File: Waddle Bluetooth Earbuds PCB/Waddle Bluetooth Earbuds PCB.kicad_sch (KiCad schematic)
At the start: 1 part, among them U1 DFR0781_BT401

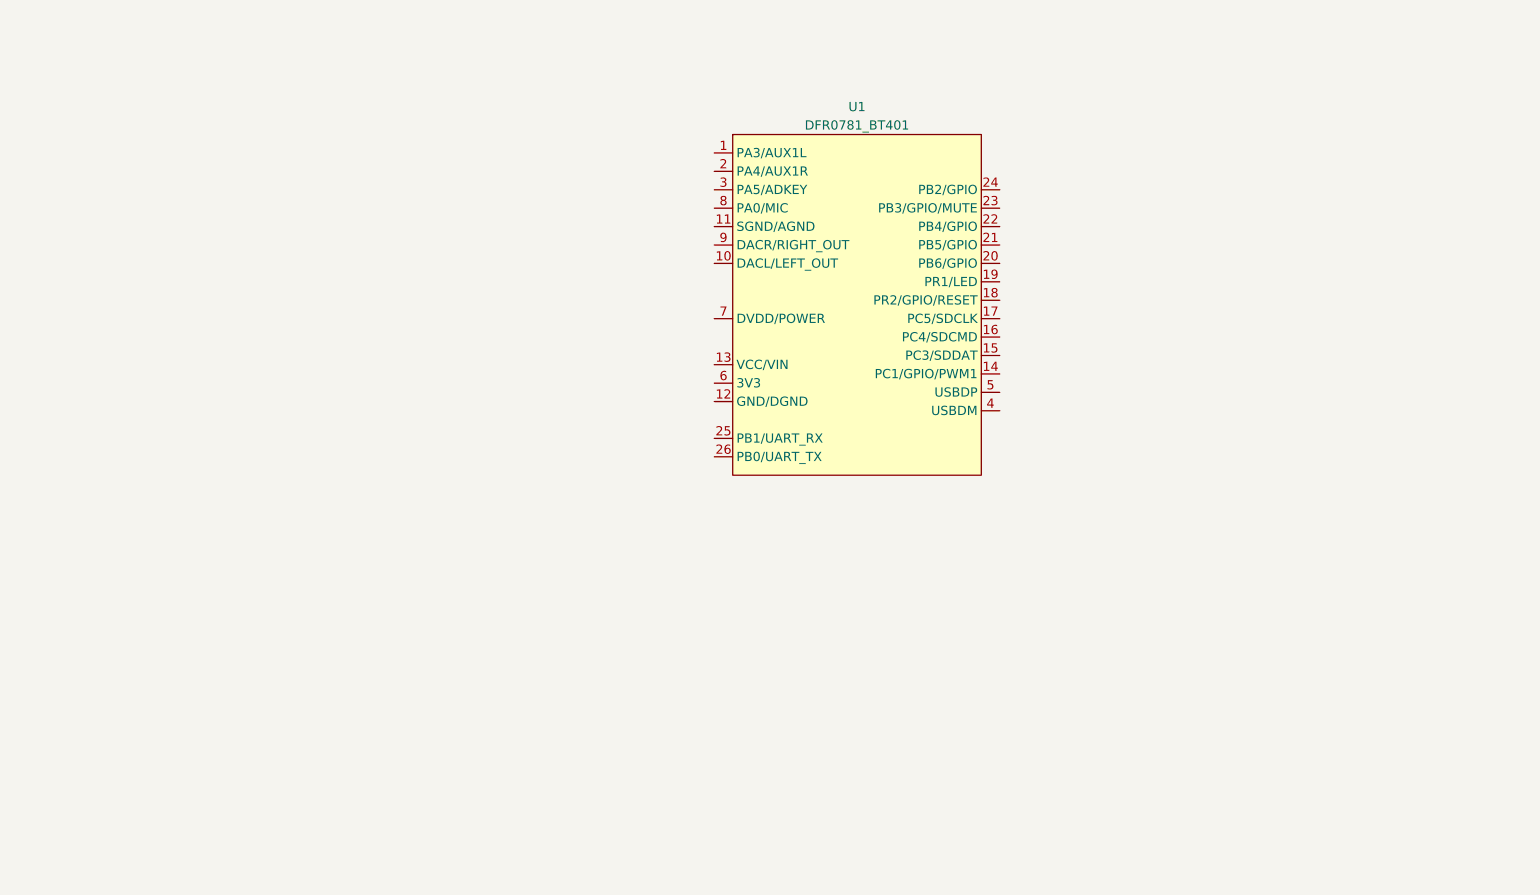
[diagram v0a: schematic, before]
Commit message: Add core bluetooth circuits
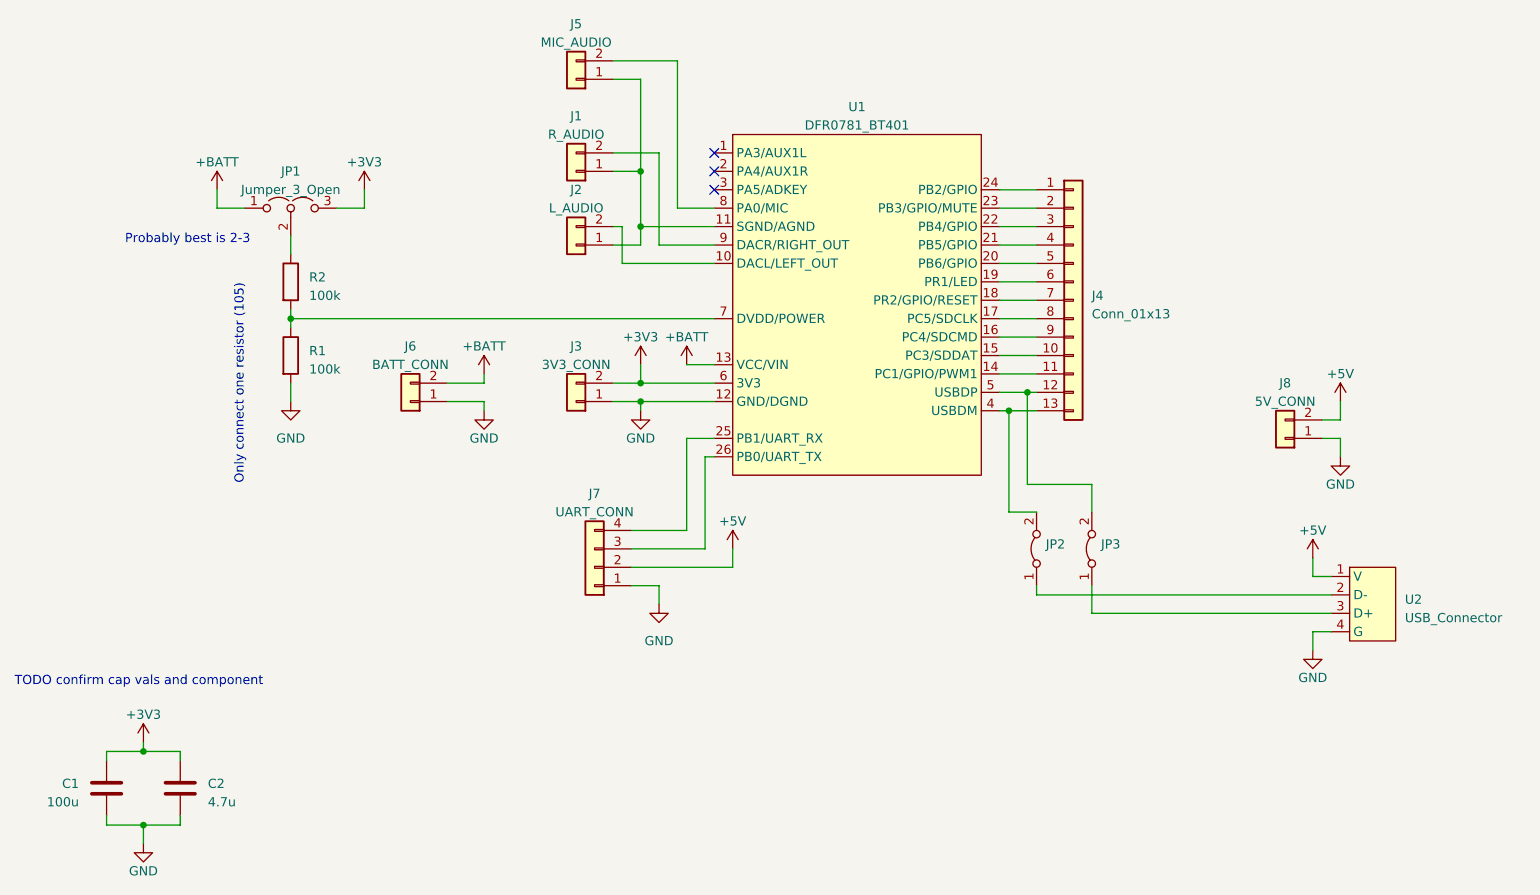
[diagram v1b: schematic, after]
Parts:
- added C1: 100u, Capacitor_SMD:C_1206_3216Metric_Pad1.33x1.80mm_HandSolder, symbol Device:C
- added C2: 4.7u, Capacitor_SMD:C_1206_3216Metric_Pad1.33x1.80mm_HandSolder, symbol Device:C
- added J1: R_AUDIO, Connector_PinHeader_1.27mm:PinHeader_1x02_P1.27mm_Vertical, symbol Connector_Generic:Conn_01x02
- added J2: L_AUDIO, Connector_PinHeader_1.27mm:PinHeader_1x02_P1.27mm_Vertical, symbol Connector_Generic:Conn_01x02
- added J3: 3V3_CONN, Connector_PinHeader_1.27mm:PinHeader_1x02_P1.27mm_Vertical, symbol Connector_Generic:Conn_01x02
- added J4: Conn_01x13, Connector_PinHeader_1.27mm:PinHeader_1x13_P1.27mm_Vertical, symbol Connector_Generic:Conn_01x13
- added J5: MIC_AUDIO, Connector_PinHeader_1.27mm:PinHeader_1x02_P1.27mm_Vertical, symbol Connector_Generic:Conn_01x02
- added J6: BATT_CONN, Connector_PinHeader_1.27mm:PinHeader_1x02_P1.27mm_Vertical, symbol Connector_Generic:Conn_01x02
- added J7: UART_CONN, Connector_PinHeader_1.27mm:PinHeader_1x04_P1.27mm_Vertical, symbol Connector_Generic:Conn_01x04
- added J8: 5V_CONN, Connector_PinHeader_1.27mm:PinHeader_1x02_P1.27mm_Vertical, symbol Connector_Generic:Conn_01x02
- added JP1: Jumper_3_Open, Jumper:SolderJumper-3_P1.3mm_Open_RoundedPad1.0x1.5mm_NumberLabels, symbol Jumper:Jumper_3_Open
- added JP2, JP3: Jumper_2_Bridged, Jumper:SolderJumper-2_P1.3mm_Open_RoundedPad1.0x1.5mm, symbol Jumper:Jumper_2_Bridged
- added R1, R2: 100k, Resistor_SMD:R_1206_3216Metric_Pad1.30x1.75mm_HandSolder, symbol Device:R
- added U2: USB_Connector, symbol Waddle_Symbol_Library:USB_Connector
- U1: footprint (none) -> Waddle_Footprint_Library:DFR0781_BT401_V3
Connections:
- net at U1.10 (DACL/LEFT_OUT): now also J2.2 (Pin_2)
- net at U1.11 (SGND/AGND): now also J1.1 (Pin_1), J2.1 (Pin_1), J5.1 (Pin_1)
- net GND: now reaches U1.12 (GND/DGND)
- net GND: now also C1.2, C2.2, J3.1 (Pin_1), J6.1 (Pin_1), J7.1 (Pin_1), J8.1 (Pin_1), R1.2, U2.4 (G)
- net +BATT: now reaches U1.13 (VCC/VIN)
- net +BATT: now also J6.2 (Pin_2), JP1.1 (A)
- net at U1.14 (PC1/GPIO/PWM1): now also J4.11 (Pin_11)
- net at U1.15 (PC3/SDDAT): now also J4.10 (Pin_10)
- net at U1.16 (PC4/SDCMD): now also J4.9 (Pin_9)
- net at U1.17 (PC5/SDCLK): now also J4.8 (Pin_8)
- net at U1.18 (PR2/GPIO/RESET): now also J4.7 (Pin_7)
- net at U1.19 (PR1/LED): now also J4.6 (Pin_6)
- net at U1.20 (PB6/GPIO): now also J4.5 (Pin_5)
- net at U1.21 (PB5/GPIO): now also J4.4 (Pin_4)
- net at U1.22 (PB4/GPIO): now also J4.3 (Pin_3)
- net at U1.23 (PB3/GPIO/MUTE): now also J4.2 (Pin_2)
- net at U1.24 (PB2/GPIO): now also J4.1 (Pin_1)
- net at U1.25 (PB1/UART_RX): now also J7.4 (Pin_4)
- net at U1.26 (PB0/UART_TX): now also J7.3 (Pin_3)
- net at U1.4 (USBDM): now also J4.13 (Pin_13), JP2.2 (B)
- net at U1.5 (USBDP): now also J4.12 (Pin_12), JP3.2 (B)
- net +3V3: now reaches U1.6 (3V3)
- net +3V3: now also C1.1, C2.1, J3.2 (Pin_2), JP1.3 (B)
- net at U1.7 (DVDD/POWER): now also R1.1, R2.2
- net at U1.8 (PA0/MIC): now also J5.2 (Pin_2)
- net at U1.9 (DACR/RIGHT_OUT): now also J1.2 (Pin_2)
- new net: JP2.1 (A), U2.2 (D-)
- new net: JP3.1 (A), U2.3 (D+)
- new net: JP1.2 (C), R2.1
- new net +5V: J7.2 (Pin_2), J8.2 (Pin_2), U2.1 (V)
- no-connect marks 0 -> 3
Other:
- note added: "Only connect one resistor (105)"
- note added: "Probably best is 2-3"
- note added: "TODO confirm cap vals and component"
